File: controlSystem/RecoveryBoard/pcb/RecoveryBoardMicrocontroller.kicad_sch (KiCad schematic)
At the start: 79 parts, among them J11 Conn_01x03, J4 J-TE-Debug-2-1734592-0, J5 Conn_01x03, J6 Sensor Board 1, J7 Sensor Board 2, J9 Motor, Q2 BSS123, U1 STM32F091C, U4 TCMT1107, U5 TCMT1107, U6 INA185, U7 TCAN330, U8 BDS63150AFM-E2, X1 16MHZ-2.5x2mm

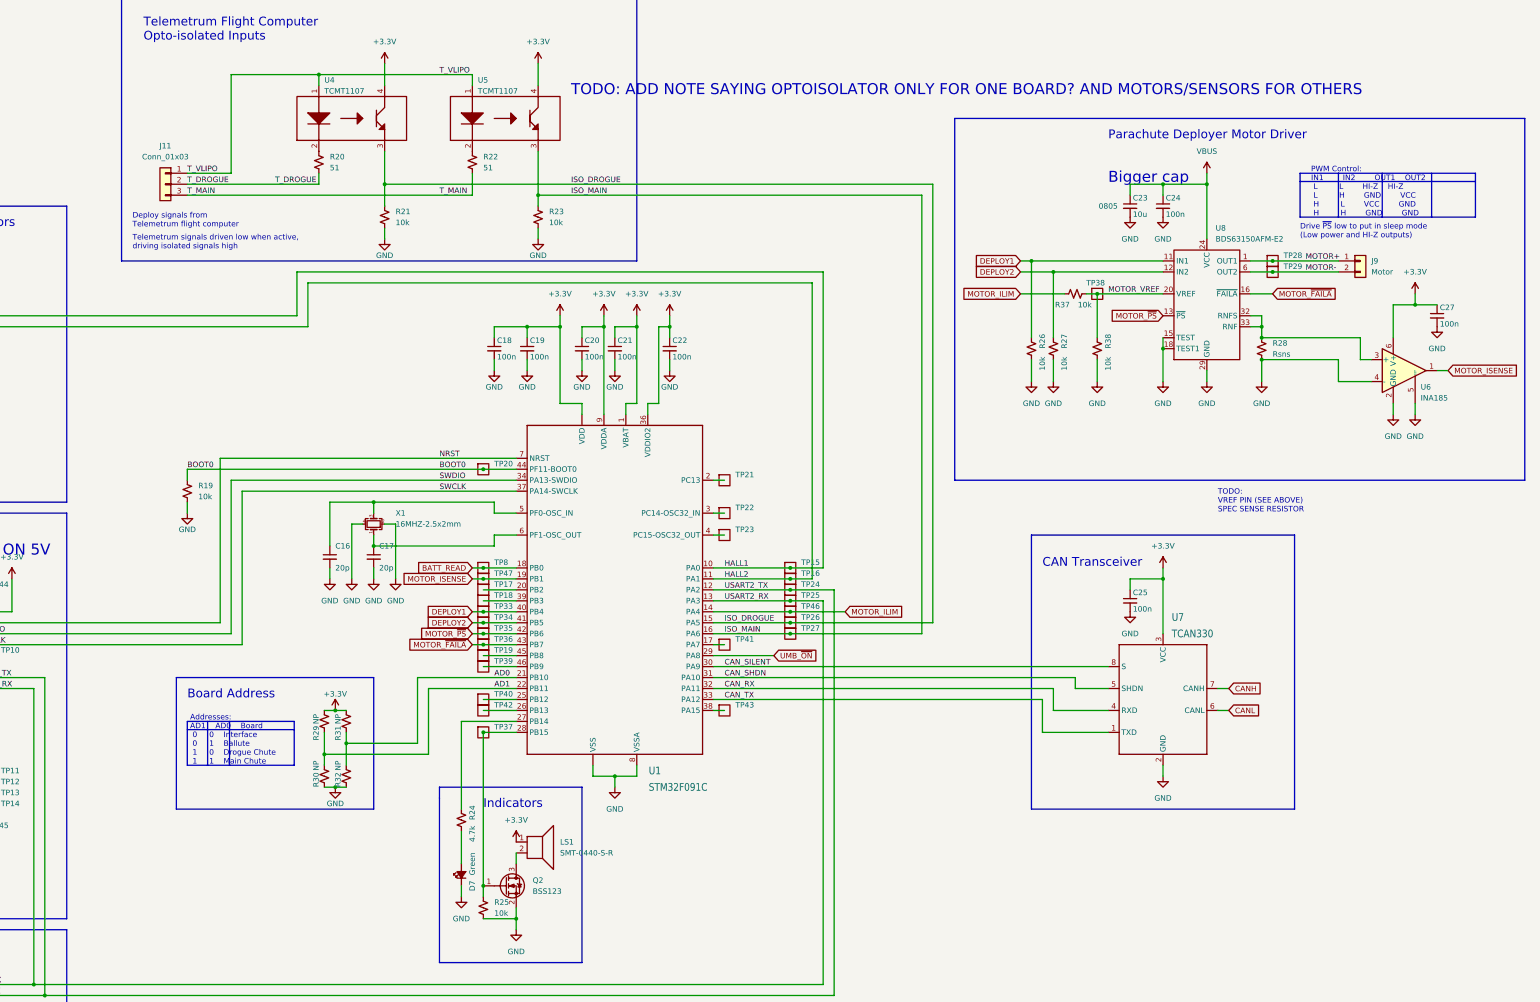
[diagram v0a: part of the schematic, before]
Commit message: Added rocket ready connector to ERS board
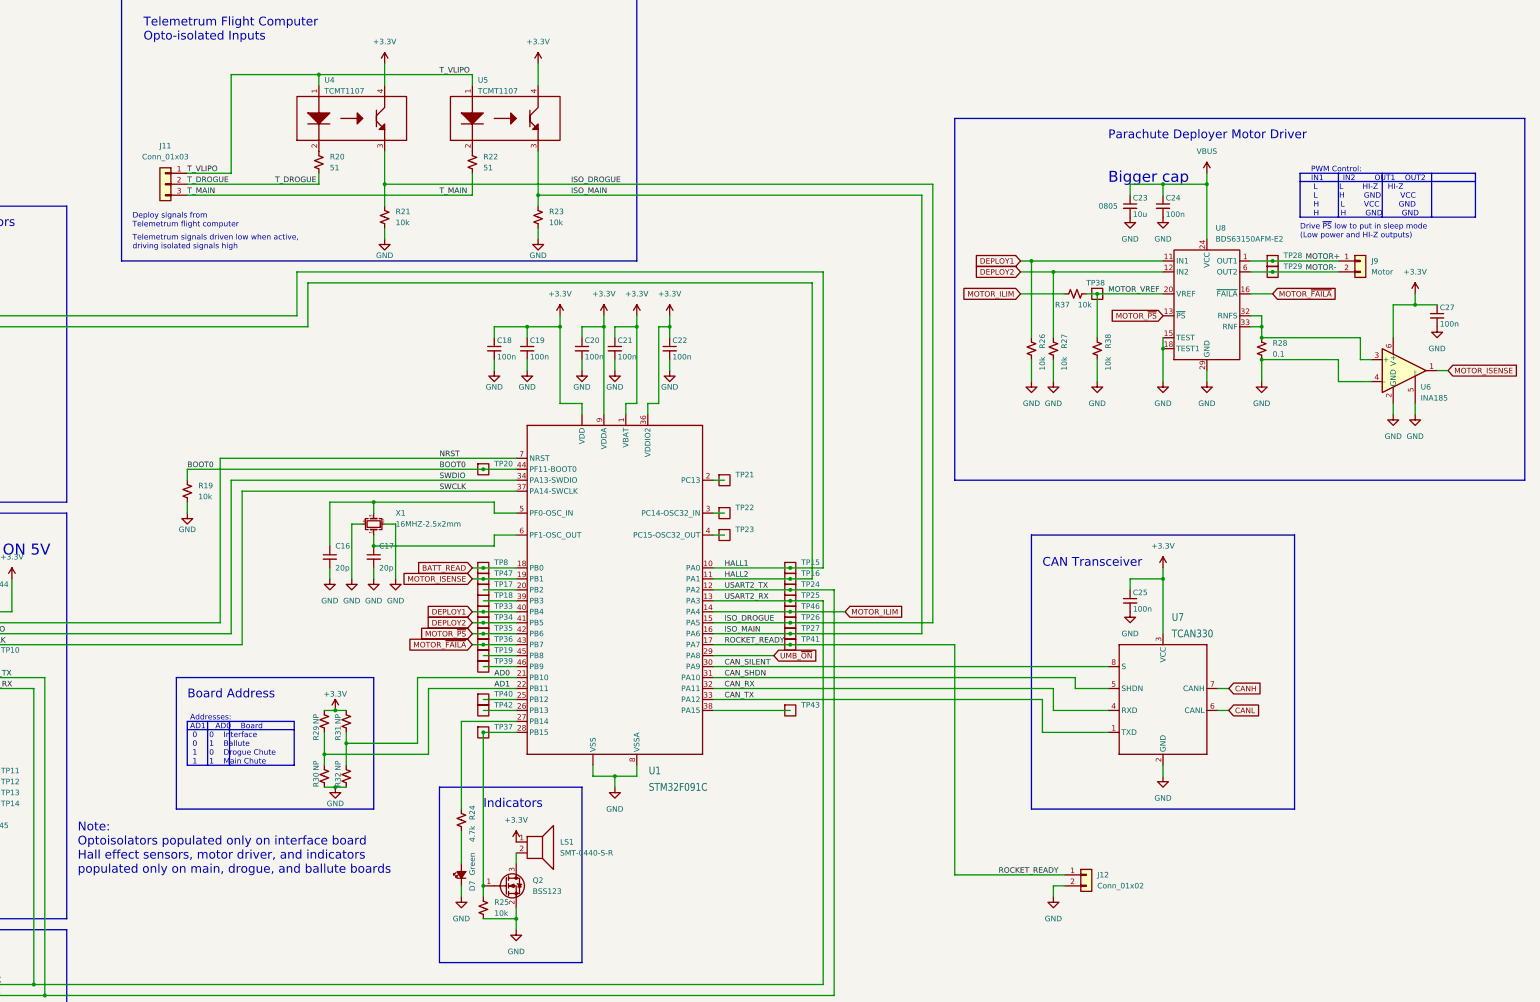
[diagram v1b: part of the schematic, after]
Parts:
- added J12: Conn_01x02, Connector_Molex:Molex_KK-254_AE-6410-02A_1x02_P2.54mm_Vertical, symbol Connector_Generic:Conn_01x02
- R28: value Rsns -> 0.1
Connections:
- net GND: now also J12.2 (Pin_2)
- net ROCKET_READY: now reaches TP41.1, U1.17 (PA7)
- net ROCKET_READY: now also J12.1 (Pin_1)
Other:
- note added: "Note: Optoisolators populated only on interface board Hall effect sensors, motor driver, and indicators populated only on main, drogue, and ballute boards"
- note removed: "TODO: ADD NOTE SAYING OPTOISOLATOR ONLY FOR ONE BOARD? AND MOTORS/SENSORS FOR OTHERS"
- note removed: "TODO: VREF PIN (SEE ABOVE) SPEC SENSE RESISTOR"
- moved on the sheet: TP41, TP43
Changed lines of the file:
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@@
   (junction (at 299.72 76.2) (diameter 0) (color 0 0 0 0)
   )
+  (junction (at 243.84 165.1) (diameter 0) (color 0 0 0 0)
+  )
   (junction (at 243.84 154.94) (diameter 0) (color 0 0 0 0)
   )
@@
     (stroke (width 0) (type default) (color 0 0 0 0))
   )
+  (wire (pts (xy 281.94 218.44) (xy 307.34 218.44))
+    (stroke (width 0) (type default) (color 0 0 0 0))
+  )
   (polyline (pts (xy 76.2 134.62) (xy 76.2 228.6))
     (stroke (width 0) (type default) (color 0 0 0 0))
@@
     (stroke (width 0) (type default) (color 0 0 0 0))
   )
-  (wire (pts (xy 226.06 180.34) (xy 228.6 180.34))
-    (stroke (width 0) (type default) (color 0 0 0 0))
-  )
   (wire (pts (xy 299.72 99.06) (xy 299.72 104.14))
     (stroke (width 0) (type default) (color 0 0 0 0))
@@
     (stroke (width 0) (type default) (color 0 0 0 0))
   )
+  (wire (pts (xy 304.8 220.98) (xy 307.34 220.98))
+    (stroke (width 0) (type default) (color 0 0 0 0))
+  )
   (wire (pts (xy 180.34 228.6) (xy 180.34 231.14))
     (stroke (width 0) (type default) (color 0 0 0 0))
   )
+  (wire (pts (xy 226.06 180.34) (xy 243.84 180.34))
+    (stroke (width 0) (type default) (color 0 0 0 0))
+  )
   (wire (pts (xy 132.08 81.28) (xy 248.92 81.28))
     (stroke (width 0) (type default) (color 0 0 0 0))
@@
     (stroke (width 0) (type default) (color 0 0 0 0))
   )
+  (wire (pts (xy 304.8 223.52) (xy 304.8 220.98))
+    (stroke (width 0) (type default) (color 0 0 0 0))
+  )
   (wire (pts (xy 135.89 190.5) (xy 160.02 190.5))
     (stroke (width 0) (type default) (color 0 0 0 0))
@@
     (stroke (width 0) (type default) (color 0 0 0 0))
   )
+  (wire (pts (xy 281.94 165.1) (xy 281.94 218.44))
+    (stroke (width 0) (type default) (color 0 0 0 0))
+  )
   (wire (pts (xy 180.34 134.62) (xy 175.26 134.62))
     (stroke (width 0) (type default) (color 0 0 0 0))
@@
     (stroke (width 0) (type default) (color 0 0 0 0))
   )
-  (wire (pts (xy 226.06 165.1) (xy 228.6 165.1))
+  (wire (pts (xy 226.06 165.1) (xy 243.84 165.1))
     (stroke (width 0) (type default) (color 0 0 0 0))
   )
@@
     (stroke (width 0) (type default) (color 0 0 0 0))
   )
+  (wire (pts (xy 243.84 165.1) (xy 281.94 165.1))
+    (stroke (width 0) (type default) (color 0 0 0 0))
+  )
   (wire (pts (xy 185.42 50.8) (xy 185.42 60.96))
     (stroke (width 0) (type default) (color 0 0 0 0))
@@
     (effects (font (size 2.032 2.032)) (justify left bottom))
   )
-  (text "TODO:\nVREF PIN (SEE ABOVE)\nSPEC SENSE RESISTOR\n" (at 342.9 134.62 0)
-    (effects (font (size 1.27 1.27)) (justify left bottom))
-  )
   (text "Board Address" (at 104.14 177.8 0)
     (effects (font (size 2.032 2.032)) (justify left bottom))
@@
     (effects (font (size 1.27 1.27)) (justify left bottom))
   )
+  (text "Note:\nOptoisolators populated only on interface board\nHall effect sensors, motor driver, and indicators\npopulated only on main, drogue, and ballute boards"
+    (at 78.74 218.44 0)
+    (effects (font (size 2.032 2.032)) (justify left bottom))
+  )
   (text "Telemetrum Flight Computer\nOpto-isolated Inputs" (at 93.98 25.4 0)
     (effects (font (size 2.032 2.032)) (justify left bottom))
@@
     (effects (font (size 2.032 2.032)) (justify left bottom))
   )
-  (text "TODO: ADD NOTE SAYING OPTOISOLATOR ONLY FOR ONE BOARD? AND MOTORS/SENSORS FOR OTHERS"
-    (at 193.04 38.1 0)
-    (effects (font (size 2.54 2.54)) (justify left bottom))
-  )
   (text "Debug Connector" (at 35.56 139.7 0)
     (effects (font (size 2.032 2.032)) (justify left bottom))
@@
     (effects (font (size 1.27 1.27)) (justify left bottom))
   )
+  (label "ROCKET_READY" (at 228.6 165.1 0)
+    (effects (font (size 1.27 1.27)) (justify left bottom))
+  )
   (label "ISO_DROGUE" (at 193.04 58.42 0)
     (effects (font (size 1.27 1.27)) (justify left bottom))
@@
     (effects (font (size 1.27 1.27)) (justify left bottom))
   )
+  (label "ROCKET_READY" (at 292.1 218.44 0)
+    (effects (font (size 1.27 1.27)) (justify left bottom))
+  )
   (label "CAN_SHDN" (at 228.6 172.72 0)
     (effects (font (size 1.27 1.27)) (justify left bottom))
@@
     (pin "2")
   )
+  (symbol (lib_id "Connector_Generic:Conn_01x02") (at 312.42 218.44 0) (unit 1)
+    (in_bom yes) (on_board yes) (fields_autoplaced)
+    (property "Reference" "J12" (id 0) (at 314.96 218.4399 0)
+      (effects (font (size 1.27 1.27)) (justify left))
+    )
+    (property "Value" "Conn_01x02" (id 1) (at 314.96 220.9799 0)
+      (effects (font (size 1.27 1.27)) (justify left))
+    )
+    (property "Footprint" "Connector_Molex:Molex_KK-254_AE-6410-02A_1x02_P2.54mm_Vertical" (id 2) (at 312.42 218.44 0)
+      (effects (font (size 1.27 1.27)) hide)
+    )
+    (property "Datasheet" "~" (id 3) (at 312.42 218.44 0)
+      (effects (font (size 1.27 1.27)) hide)
+    )
+    (pin "1")
+    (pin "2")
+  )
   (symbol (lib_id "psas-testpoint:Test-Point") (at 172.72 152.4 0) (unit 1)
     (in_bom yes) (on_board yes)
@@
     (pin "1")
   )
-  (symbol (lib_id "psas-testpoint:Test-Point") (at 228.6 165.1 0) (unit 1)
+  (symbol (lib_id "psas-testpoint:Test-Point") (at 243.84 165.1 0) (unit 1)
     (in_bom yes) (on_board yes)
-    (property "Reference" "TP41" (id 0) (at 231.14 163.83 0)
+    (property "Reference" "TP41" (id 0) (at 246.38 163.83 0)
       (effects (font (size 1.27 1.27)) (justify left))
     )
-    (property "Value" "Test-Point" (id 1) (at 228.6 162.56 0)
+    (property "Value" "Test-Point" (id 1) (at 243.84 162.56 0)
       (effects (font (size 1.27 1.27)) hide)
     )
-    (property "Footprint" "psas-footprints:TP-through-hole-1X01" (id 2) (at 228.6 162.56 0)
+    (property "Footprint" "psas-footprints:TP-through-hole-1X01" (id 2) (at 243.84 162.56 0)
       (effects (font (size 1.27 1.27)) hide)
     )
-    (property "Datasheet" "" (id 3) (at 228.6 162.56 0)
+    (property "Datasheet" "" (id 3) (at 243.84 162.56 0)
       (effects (font (size 1.27 1.27)) hide)
     )
@@
       (effects (font (size 1.27 1.27)) (justify left))
     )
-    (property "Value" "Rsns" (id 1) (at 355.6 97.7899 0)
+    (property "Value" "0.1" (id 1) (at 355.6 97.7899 0)
       (effects (font (size 1.27 1.27)) (justify left))
     )
@@
     (pin "1")
   )
+  (symbol (lib_id "power:GND") (at 304.8 223.52 0) (unit 1)
+    (in_bom yes) (on_board yes) (fields_autoplaced)
+    (property "Reference" "#PWR0113" (id 0) (at 304.8 229.87 0)
+      (effects (font (size 1.27 1.27)) hide)
+    )
+    (property "Value" "GND" (id 1) (at 304.8 228.6 0))
+    (property "Footprint" "" (id 2) (at 304.8 223.52 0)
+      (effects (font (size 1.27 1.27)) hide)
+    )
+    (property "Datasheet" "" (id 3) (at 304.8 223.52 0)
+      (effects (font (size 1.27 1.27)) hide)
+    )
+    (pin "1")
+  )
   (symbol (lib_id "psas-testpoint:Test-Point") (at 243.84 147.32 0) (unit 1)
     (in_bom yes) (on_board yes)
@@
     (pin "1")
   )
-  (symbol (lib_id "psas-testpoint:Test-Point") (at 228.6 180.34 0) (unit 1)
+  (symbol (lib_id "psas-testpoint:Test-Point") (at 243.84 180.34 0) (unit 1)
     (in_bom yes) (on_board yes)
-    (property "Reference" "TP43" (id 0) (at 231.14 179.07 0)
+    (property "Reference" "TP43" (id 0) (at 246.38 179.07 0)
       (effects (font (size 1.27 1.27)) (justify left))
     )
-    (property "Value" "Test-Point" (id 1) (at 228.6 177.8 0)
+    (property "Value" "Test-Point" (id 1) (at 243.84 177.8 0)
       (effects (font (size 1.27 1.27)) hide)
     )
-    (property "Footprint" "psas-footprints:TP-through-hole-1X01" (id 2) (at 228.6 177.8 0)
+    (property "Footprint" "psas-footprints:TP-through-hole-1X01" (id 2) (at 243.84 177.8 0)
       (effects (font (size 1.27 1.27)) hide)
     )
-    (property "Datasheet" "" (id 3) (at 228.6 177.8 0)
+    (property "Datasheet" "" (id 3) (at 243.84 177.8 0)
       (effects (font (size 1.27 1.27)) hide)
     )

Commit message: Design review changes and cleaned up board layout.
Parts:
- added C28: 100u, Capacitor_Tantalum_SMD:CP_EIA-7343-43_Kemet-X, symbol Device:C_Polarized_Small_US
- added Q3: PMF170XP, Package_TO_SOT_SMD:SOT-323_SC-70, symbol Device:Q_PMOS_GSD
- added R33: 10k, Resistor_SMD:R_0603_1608Metric, symbol Device:R_Small_US
- added R34: 10, Resistor_SMD:R_0603_1608Metric, symbol Device:R_Small_US
- added R39, R40: 33m, Resistor_SMD:R_1206_3216Metric, symbol Device:R_Small_US
- LS1: footprint Inductor_SMD:L_Vishay_IHLP-1616 -> psas-footprints:SMT-0440-S-R
- R28: value 0.1 -> 33m
- U7: footprint Package_TO_SOT_SMD:SOT-23-8 -> psas-footprints:SOT23-8
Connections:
- net +3.3V: now also Q3.2 (S), R33.2
- net GND: now also C28.2, R40.2; no longer R28.2, U6.4 (-)
- net ROCKET_READY: now also Q3.1 (G), R33.1; no longer J12.1 (Pin_1)
- net VBUS: now also C28.1
- net at R28.1, U8.32 (RNFS), U8.33 (RNF)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: no longer U6.3 (+)
- net SDWIO renamed SWDIO
- new net: R28.2, R39.1, U6.3 (+)
- new net: R39.2, R40.1, U6.4 (-)
- new net: J12.1 (Pin_1), R34.2
- new net: Q3.3 (D), R34.1
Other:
- note removed: "Bigger cap"
- moved on the sheet: C27, J12, R28

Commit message: v3.1. Cap to deal with spikes on RBF, 100k on main Q pull down, better notes on schematic for part numbers, moved Vbatt pickoff to after main Q.
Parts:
- D7: value Green -> GRN
- J11, J5: value Conn_01x03 -> 0022-232031
- J12: value Conn_01x02 -> 0022-232021
- J6: value Sensor Board 1 -> 0022-232031
- J7: value Sensor Board 2 -> 0022-232031
- J9: value Motor -> 0022-232021
- U6: value INA185 -> INA185A1
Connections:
- net ROCKET_READY renamed ~{ROCKET_READY}
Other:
- note added: "Connector going to 3.5 mm jack serial port, such as TTL-232R-3V3-AJ or equivalent. 3.5 mm bulkhead mount jack is Schurter 4832.2300."
- note added: "MOTOR_ISENSE voltage = I * 0.033 * 20 + 0 Thus I = MOTOR_ISENSE / 0.66 (Max current is 3.3V / 0.66 = 5 A)"
- note added: "Max current: MOTOR_ILIM = 3.3v => VREF = 1.65V. Imax = 1.65 / 3 / 0.099 = 5.6 A MOTOR_ILIM(V) Imax(A) 1.0 V 1.7 A 2.0 V 3.4 A 3.0 V 5.1 A"
- note added: "Motor: Pololu #3205 47:1 gear, 12V, 5A"
- note added: "TODO: buzzer too quiet!"
- note removed: "CAP ON 5V"
- note removed: "Connector going to 3.5 mm jack serial port"
- title: (none) -> Electromechanical Recovery System Board
- moved on the sheet: C23, C24, C27, C28, J9, R24, R26, R27, R28, R37, R38, R39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

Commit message: Stuffing four more v3.0 PCBs and discovered everything wasn't updated. Fixed BOM, fixed a lot of schematic errors especially in symbols, fixed some footprint errors, synchronized schematic and pcb, and general cleanup. This board is still v3.1.
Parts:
- C16, C17: DPN (none) -> 399-C0603C200G4HAC7867CT-ND; DST (none) -> DigiKey; MFR (none) -> Kemet; MPN (none) -> C0603C200G4HAC7867
- C18, C19, C20, C21, C22, C24, C25, C27: DPN (none) -> 1276-6854-1-ND; DST (none) -> DigiKey; MFR (none) -> Samsung Microelectronics; MPN (none) -> CL10B104KB8WPNC
- C23: DPN (none) -> 490-18663-1-ND; DST (none) -> DigiKey; Field4 0805 -> (none); MFR (none) -> Murata; MPN (none) -> GRM21BR61H106KE43L
- C28: DPN (none) -> 399-8409-1-ND; DST (none) -> DigiKey; Field4 Tantalum 25V -> (none); MFR (none) -> Kemet; MPN T491X107K025AT -> T491X107K020AT
- D7: DPN (none) -> 732-4971-1-ND; DST (none) -> DigiKey; MFR (none) -> Wurth; MPN (none) -> 150060GS75000
- J11, J5, J6, J7: DPN (none) -> WM4201-ND; DST (none) -> DigiKey; MFR (none) -> Molex; MPN (none) -> 22232031
- J12, J9: DPN (none) -> 900-0022232021-ND; DST (none) -> DigiKey; MFR (none) -> Molex; MPN (none) -> 22232021
- J4: DPN (none) -> A100287CT-ND; DST (none) -> DigiKey; MFR (none) -> TE; MPN (none) -> 2-1734592-0
- LS1: DPN (none) -> 668-1488-1-ND; DST (none) -> DigiKey; MFR (none) -> PUI Audio
- Q2: DPN (none) -> BSS123NCT-ND; DST (none) -> DigiKey; MFR (none) -> onsemi; MPN (none) -> BSS123
- Q3: DPN (none) -> 1727-1229-1-ND; DST (none) -> DigiKey; MFR (none) -> Nexperia; MPN (none) -> PMF170XP,115
- R19, R21, R23, R25, R26, R27, R33, R37, R38: DPN (none) -> 311-10.0KHRCT-ND; DST (none) -> DigiKey; MFR (none) -> Yageo; MPN (none) -> RC0603FR-0710KL
- R20, R22: DPN (none) -> 311-51.0HRCT-ND; DST (none) -> DigiKey; MFR (none) -> Yageo; MPN (none) -> RC0603FR-0751RL
- R24: DPN (none) -> 311-4.70KHRCT-ND; DST (none) -> DigiKey; MFR (none) -> Yageo; MPN (none) -> RC0603FR-074K7L
- R28, R39, R40: DPN (none) -> A109633CT-ND; DST (none) -> DigiKey; MFR (none) -> Stackpole; MPN (none) -> RLP73M2BR033FTDF
- R29, R30, R31, R32: now not fitted
- R34: DPN (none) -> 311-10.0HRCT-ND; DST (none) -> DigiKey; MFR (none) -> Yageo; MPN (none) -> RC0603FR-0710RL
- TP10, TP11, TP12, TP13, TP14, TP15, TP16, TP17, TP18, TP19, TP21, TP22, TP23, TP24, TP25, TP26, TP27, TP28, TP29, TP33, TP34, TP35, TP36, TP37, TP38, TP39, TP40, TP41, TP42, TP43, TP44, TP45, TP46, TP47, TP8: now left out of the parts list
- U1: DPN (none) -> 497-18749-1-ND; DST (none) -> DigiKey; MFR (none) -> STMicroelectronics; MPN (none) -> STM32F091CCT7
- U4, U5: DPN (none) -> TCMT1107CT-ND; DST (none) -> DigiKey; MFR (none) -> Vishay; MPN (none) -> TCMT1107
- U6: DPN (none) -> 296-INA185A1IDRLRCT-ND; DST (none) -> DigiKey; MFR (none) -> Texas Instruments; MPN (none) -> INA185A1IDRLR
- U7: DPN (none) -> 296-44211-1-ND; DST (none) -> DigiKey; Distributor DigiKey -> (none); MFR (none) -> Texas Instruments; MPN TCAN330GDCN -> TCAN330GDCNT
- U8: DPN (none) -> BD63150AFM-E2CT-ND; DST (none) -> DigiKey; MFR (none) -> Rohm; MPN (none) -> BD63150AFM-E2
- X1: DPN (none) -> XC2181CT-ND; DST (none) -> DigiKey; MFR (none) -> ECS Inc.; MPN (none) -> ECS-160-10-36Q-ES-TR
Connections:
- net GND: now also U8.22 (GND), U8.37 (GND), U8.38 (GND); no longer U8.FIN
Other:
- moved on the sheet: C23, C24, C27, C28, J9, R24, R26, R27, R28, R37, R38, R39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
